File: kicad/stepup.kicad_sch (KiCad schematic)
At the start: 9 parts, among them U1 LM2733XMF

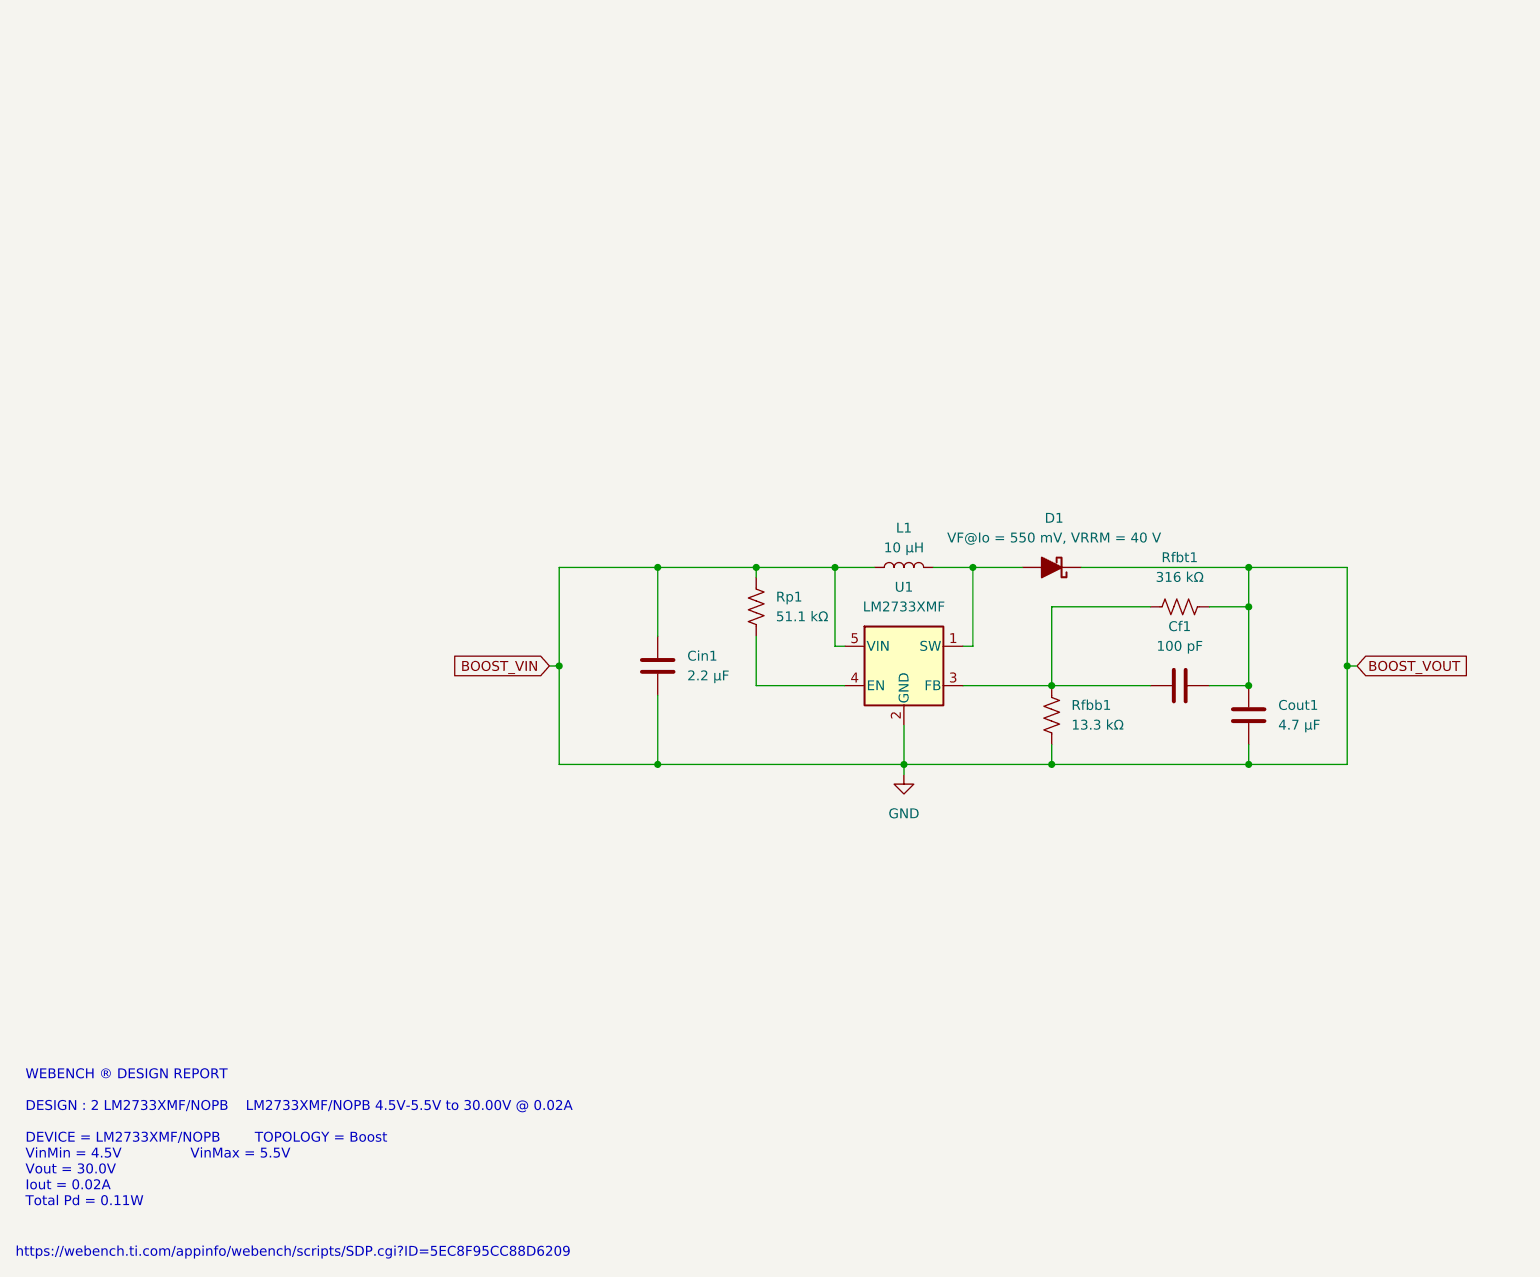
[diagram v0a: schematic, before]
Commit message: finished wiring everything but 30v
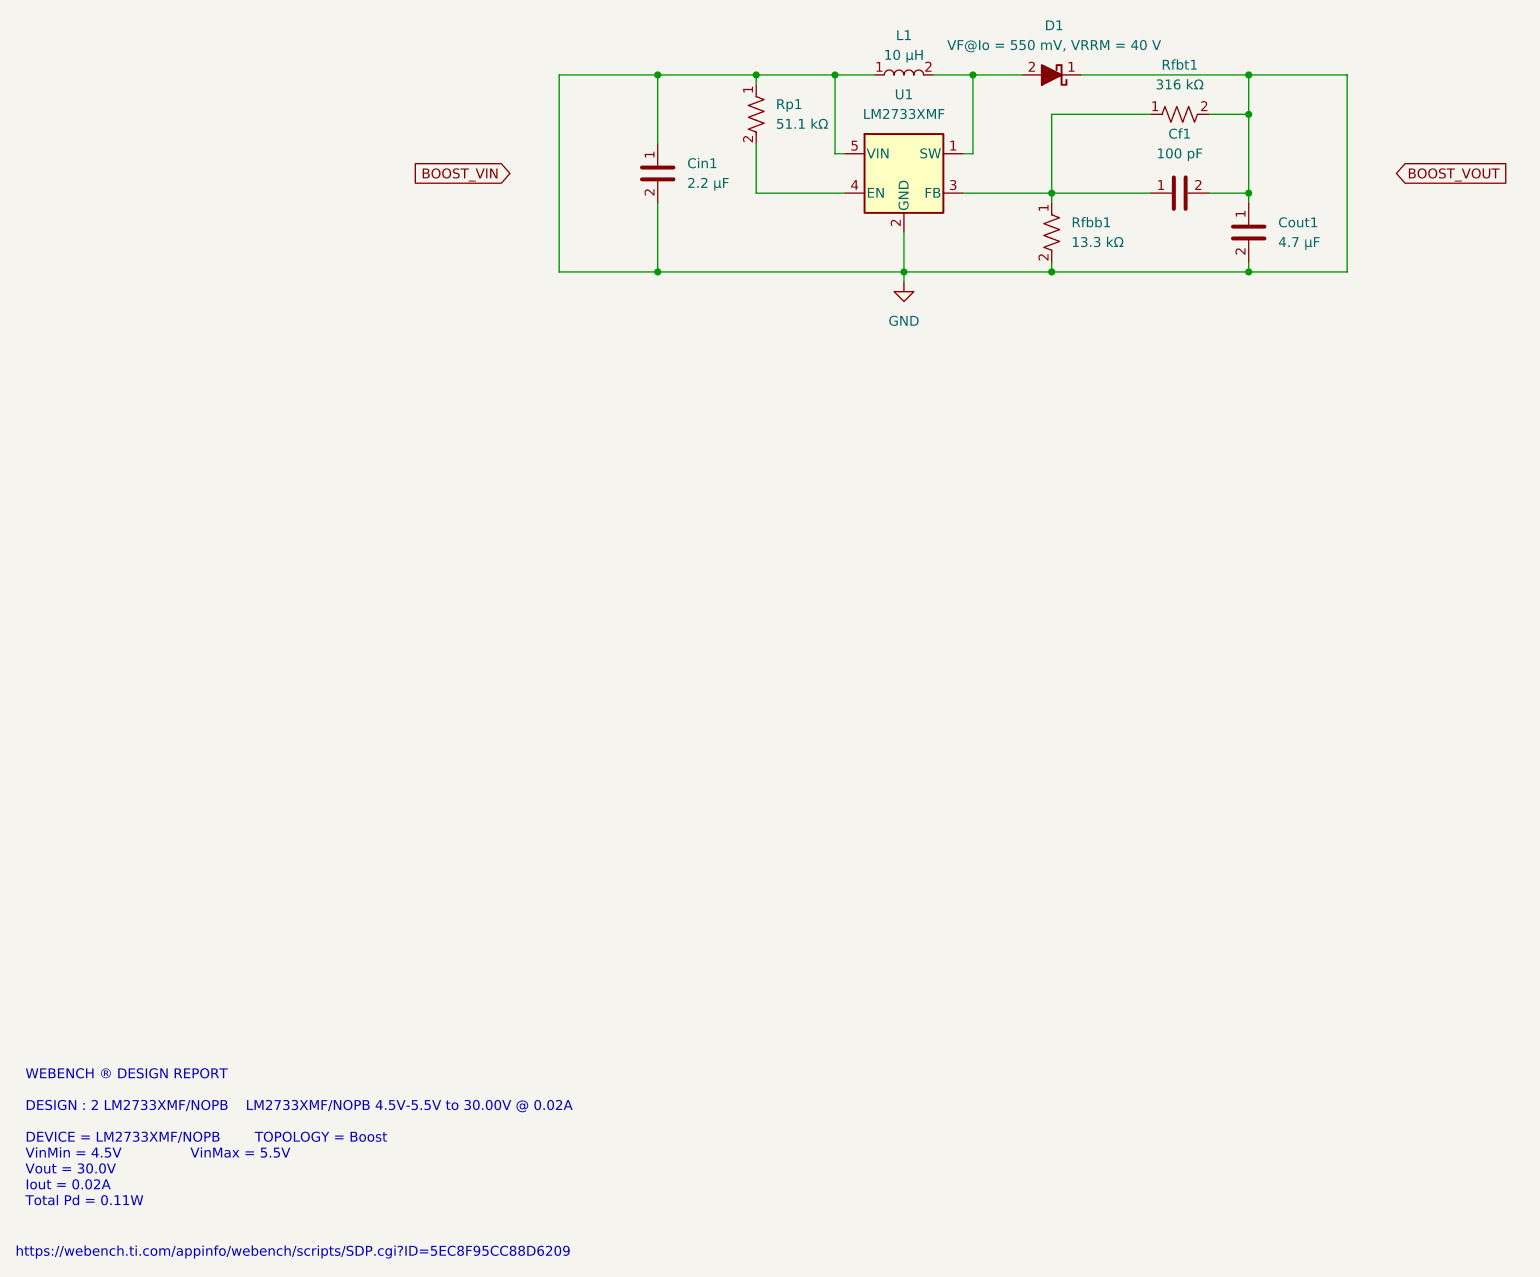
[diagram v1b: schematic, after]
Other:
- moved on the sheet: U1
